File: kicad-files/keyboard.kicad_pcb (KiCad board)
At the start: 2 copper layers, 325 x 100 mm, 185 parts, among them J1 TYPE-C-31-M12_13, Q1 2N7002, Q2 2N7002, SW1 K2-1187SQ-A4SW-06, U1 STM32F411CEU6, U2 USBLC6-2SC6, U3 AT24C256C-SSHL-T, U4 SGM2007-3.3XN5/TR, Y1 TAXM8M4RFDCET2T

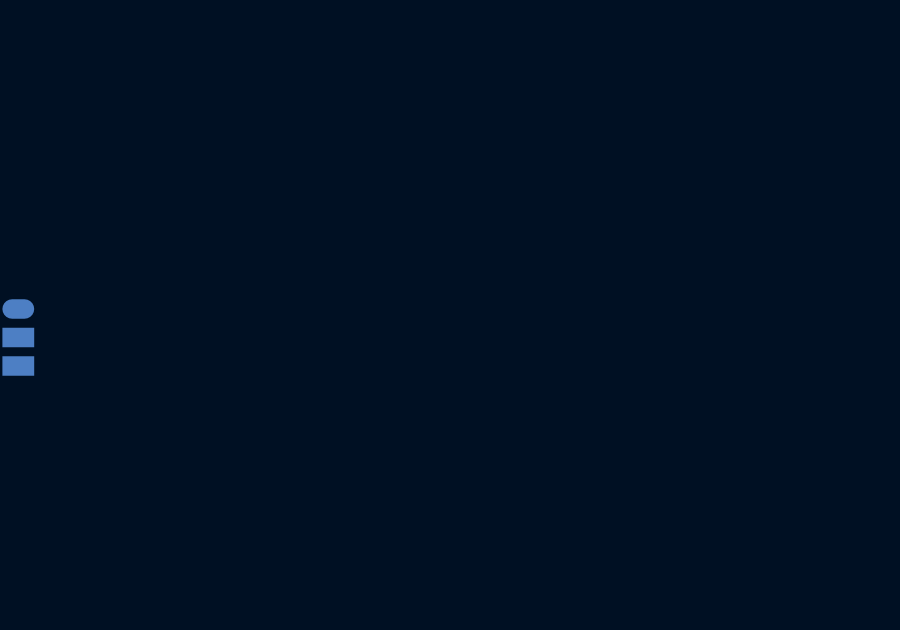
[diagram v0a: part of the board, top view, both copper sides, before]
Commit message: Added connector for DB
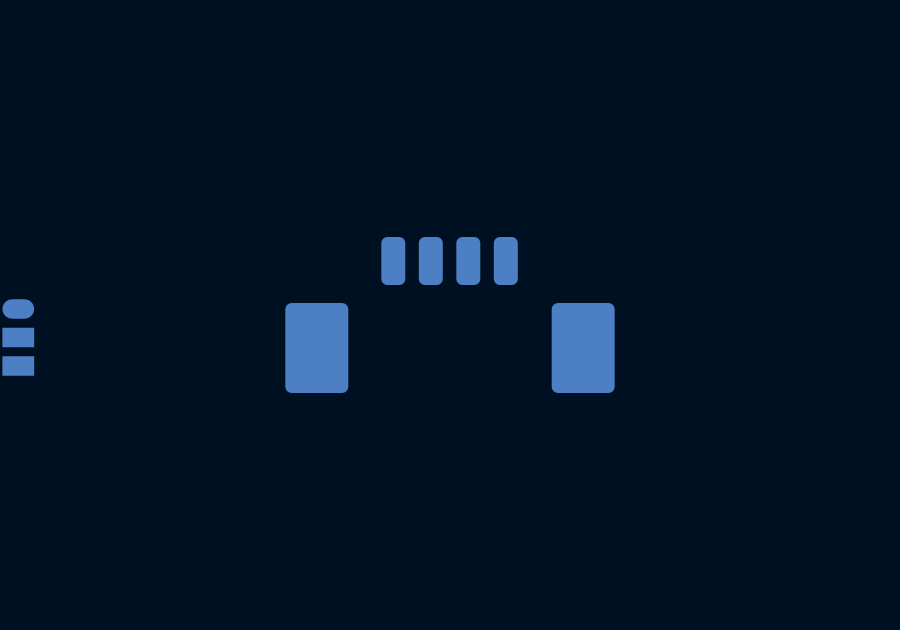
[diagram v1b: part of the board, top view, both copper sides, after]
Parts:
- added T1: 53261-0471, Legshark:Molex, PicoBlade, 53261, 4 Way, 1 Row, Right Angle PCB Header, B.Cu at (201.6, -28.7)
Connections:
- C3 pad 2: GND -> GND1
- C4 pad 2: GND -> GND1
- C5 pad 2: GND -> GND1
- FB1 pad 2: GND -> GND1
- J1 pad A1: GND -> GND1
- J1 pad B1: GND -> GND1
- R1 pad 2: GND -> GND1
- R2 pad 2: GND -> GND1
- R3 pad 1: GND -> GND1
- R4 pad 1: GND -> GND1
- SW1 pad 1: 3V3 -> unconnected-(SW1-A-Pad1)
- U2 pad 2: GND -> GND1
- U4 pad 2: GND -> GND1
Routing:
- net unconnected-(SW1-A-Pad1): track 0.00 -> 6.20 mm
- net 3V3: track 30.4 -> 24.2 mm

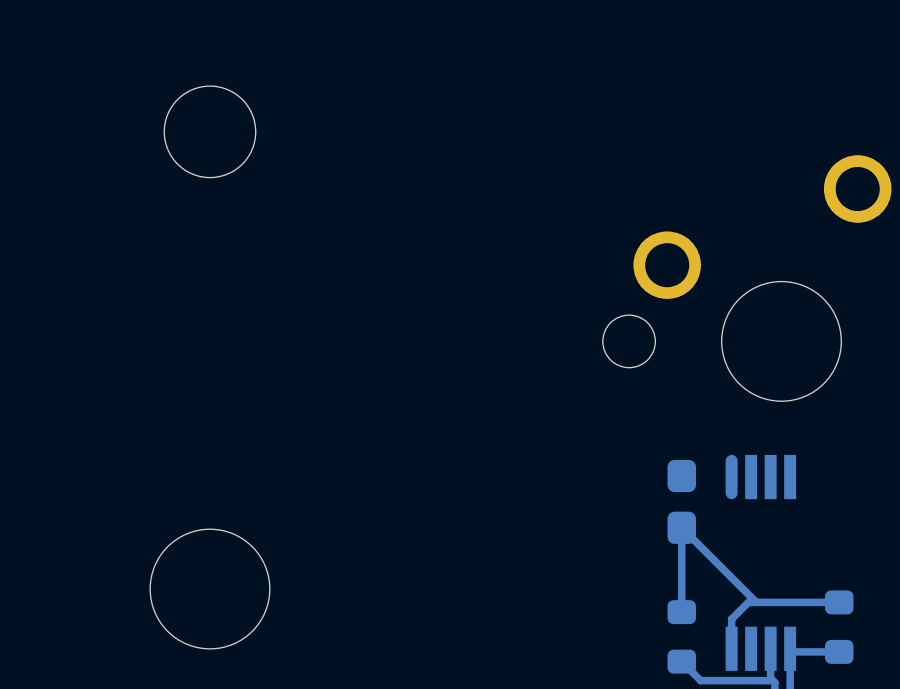
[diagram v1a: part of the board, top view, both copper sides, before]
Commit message: Added the cable header for DB to MB
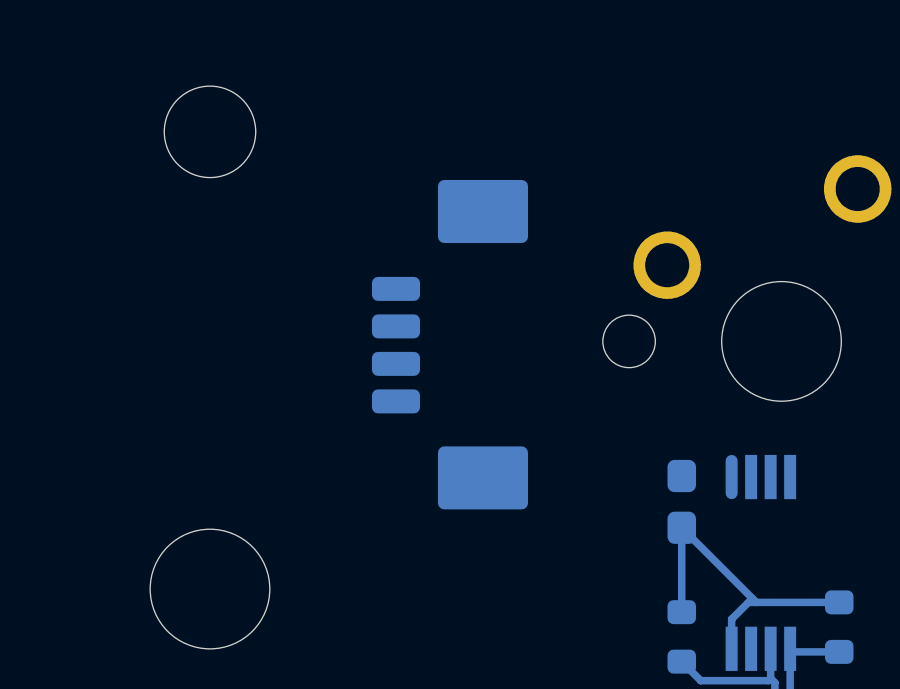
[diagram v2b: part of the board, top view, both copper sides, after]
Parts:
- added T2: 53261-0471, Legshark:Molex, PicoBlade, 53261, 4 Way, 1 Row, Right Angle PCB Header, B.Cu at (264.8, 50.3)
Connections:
- C5 pad 1: 3V3 -> Net-(D1-A)
- D1 pad 2: 3V3 -> Net-(D1-A)
- R4 pad 2: 3V3 -> Net-(D1-A)
- SW1 pad 1: unconnected-(SW1-A-Pad1) -> 3V3
- T1 pad 1: unconnected-(T1-P1-Pad1) -> Net-(D1-A)
- T1 pad 2: unconnected-(T1-P2-Pad2) -> Net-(T1-D-)
- T1 pad 3: unconnected-(T1-P3-Pad3) -> Net-(T1-D+)
- U2 pad 1: D+ -> Net-(T1-D+)
- U2 pad 3: D- -> Net-(T1-D-)
- U4 pad 5: 3V3 -> Net-(D1-A)
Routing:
- net unconnected-(SW1-A-Pad1): track 6.20 -> 0.00 mm
- net 3V3: track 24.2 -> 30.4 mm

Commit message: Added fill area for MB
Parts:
- moved D_46 16.1 mm to (310.0, 41.8)
- moved D_31 15.5 mm to (310.0, 22.8)
- moved D_15 15.3 mm to (310.2, 3.75)
- moved D_71 0.79 mm to (310.0, 80.0)
- moved T2 0.25 mm to (264.5, 50.3)
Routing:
- added copper zone on B.Cu, net GND
- added copper zone on F.Cu, net GND
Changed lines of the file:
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@@
   )
   (footprint "Diode_SMD:D_SOD-123" (layer "B.Cu")
-    (at 317 17.5)
+    (at 310.25 3.75)
     (descr "SOD-123")
     (tags "SOD-123")
@@
   )
   (footprint "Diode_SMD:D_SOD-123" (layer "B.Cu")
-    (at 316.75 36.75)
+    (at 310 22.75)
     (descr "SOD-123")
     (tags "SOD-123")
@@
   )
   (footprint "Legshark:Molex, PicoBlade, 53261, 4 Way, 1 Row, Right Angle PCB Header" (layer "B.Cu")
-    (at 264.775 50.3 -90)
+    (at 264.525 50.3 -90)
     (property "Sheetfile" "keyboard.kicad_sch")
     (property "Sheetname" "")
@@
       (polygon
         (pts
-          (xy 264.775 44.5)
-          (xy 264.775 56)
-          (xy 268.675 56)
-          (xy 268.675 44.5)
+          (xy 264.525 44.5)
+          (xy 264.525 56)
+          (xy 268.425 56)
+          (xy 268.425 44.5)
         )
       )
@@
   )
   (footprint "Diode_SMD:D_SOD-123" (layer "B.Cu")
-    (at 317 56.25)
+    (at 310 41.75)
     (descr "SOD-123")
     (tags "SOD-123")
@@
   )
   (footprint "Diode_SMD:D_SOD-123" (layer "B.Cu")
-    (at 310.75 80.25)
+    (at 310 80)
     (descr "SOD-123")
     (tags "SOD-123")
@@
   (segment (start 276.463108 60.39669) (end 276.463108 61.38419) (width 0.25) (layer "B.Cu") (net 151))
   (segment (start 276.463108 61.38419) (end 276.604919 61.526001) (width 0.25) (layer "B.Cu") (net 151))
+  (zone (net 104) (net_name "GND") (layer "F.Cu") (hatch edge 0.5)
+    (connect_pads (clearance 0.508))
+    (min_thickness 0.25) (filled_areas_thickness no)
+    (fill (thermal_gap 0.5) (thermal_bridge_width 0.5))
+    (polygon
+      (pts
+        (xy 0 0)
+        (xy 325 0)
+        (xy 325 100)
+        (xy 0 100)
+      )
+    )
+  )
+  (zone (net 104) (net_name "GND") (layer "B.Cu") (hatch edge 0.5)
+    (priority 1)
+    (connect_pads (clearance 0.508))
+    (min_thickness 0.25) (filled_areas_thickness no)
+    (fill (thermal_gap 0.5) (thermal_bridge_width 0.5))
+    (polygon
+      (pts
+        (xy 0 0)
+        (xy 325 0)
+        (xy 325 100)
+        (xy 0 100)
+      )
+    )
+  )
 )

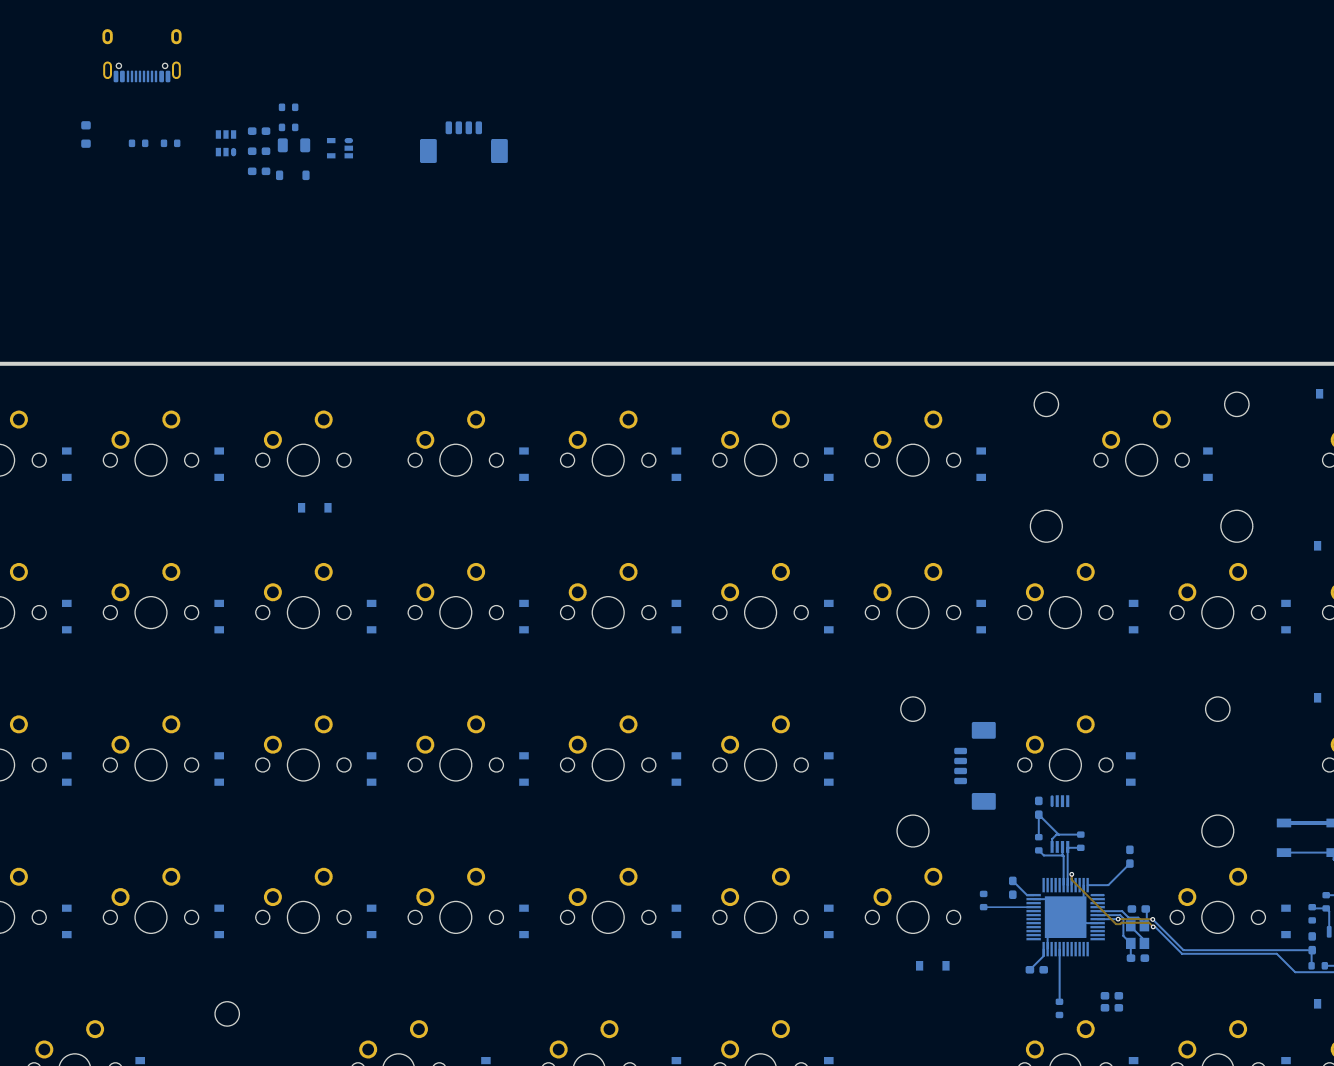
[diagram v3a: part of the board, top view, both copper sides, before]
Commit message: Connected all 3V3 to STM
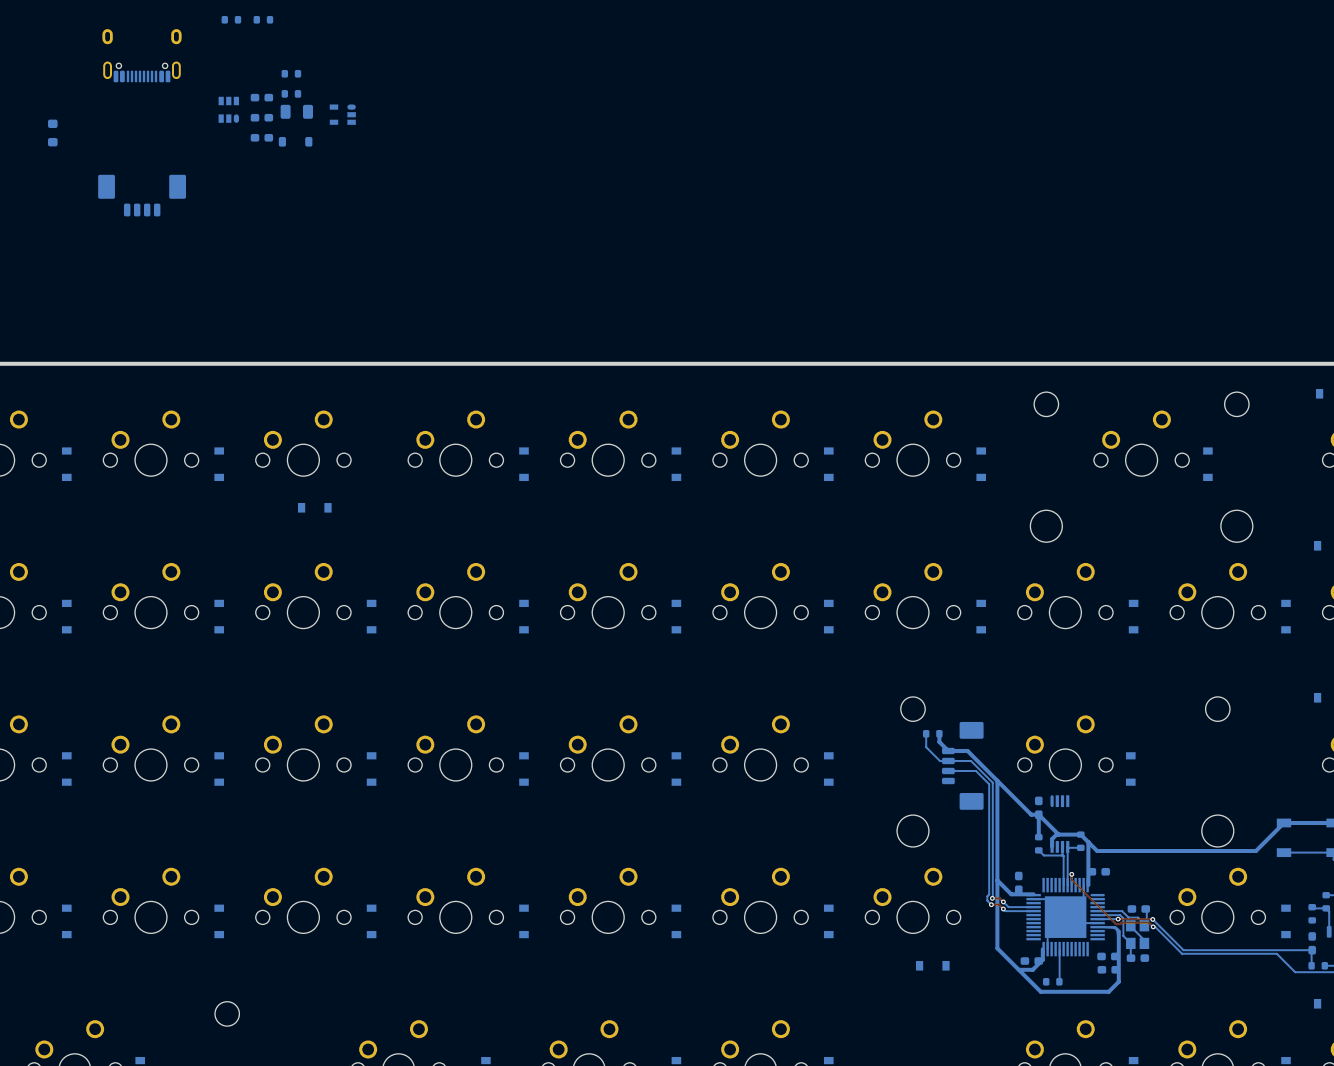
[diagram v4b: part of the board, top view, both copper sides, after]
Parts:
- moved T1 41.1 mm to (161.4, -20.0), turned to 0 degrees
- moved R5 21.8 mm to (260.2, 46.2), turned to 0 degrees
- moved R1 19.3 mm to (172.6, -43.0)
- moved R2 19.3 mm to (176.6, -43.0)
- moved C12 6.43 mm to (282.2, 74.1), turned to 0 degrees
- moved C9 4.32 mm to (281.0, 63.5), turned to 180 degrees
- moved C3 4.20 mm to (176.4, -33.3)
- moved R4 4.20 mm to (180.1, -33.7)
- moved C4 4.20 mm to (176.4, -30.8)
- moved C5 4.20 mm to (176.4, -28.2)
- moved D1 4.20 mm to (180.6, -27.8)
- moved F1 4.20 mm to (180.8, -31.5)
- moved R3 4.20 mm to (180.1, -36.2)
- moved U2 4.20 mm to (172.2, -31.8)
- moved U4 4.20 mm to (186.5, -31.1)
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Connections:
- T1 pad 2: Net-(T1-D-) -> Net-(T1-D+)
- T1 pad 3: Net-(T1-D+) -> Net-(T1-D-)
- T2 pad 2: D- -> D+
- T2 pad 3: D+ -> D-
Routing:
- net 3V3: track 30.4 -> 125.9 mm
- net D-: track 0.00 -> 26.8 mm, vias 0 -> 2
- net D+: track 6.25 -> 31.9 mm, vias 0 -> 2
- net Net-(U1-PB2--BOOT1): track 6.59 -> 4.10 mm
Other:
- board text added: "HARD RESET"

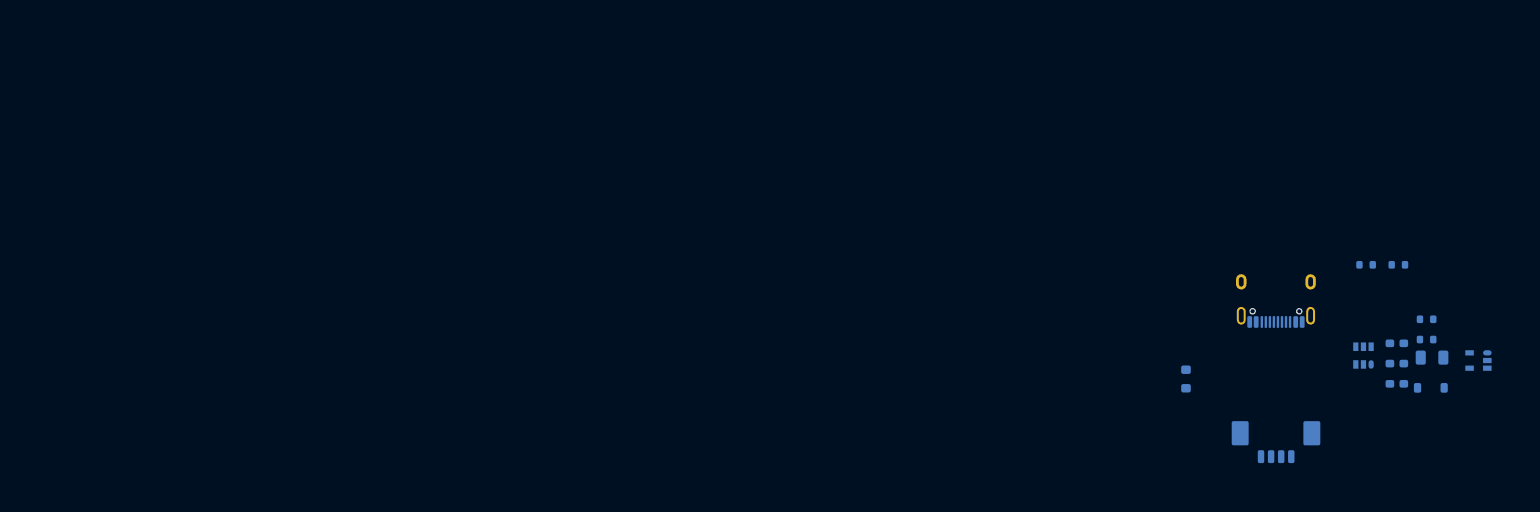
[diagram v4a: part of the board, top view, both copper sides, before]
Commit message: Started piecing together daughter board
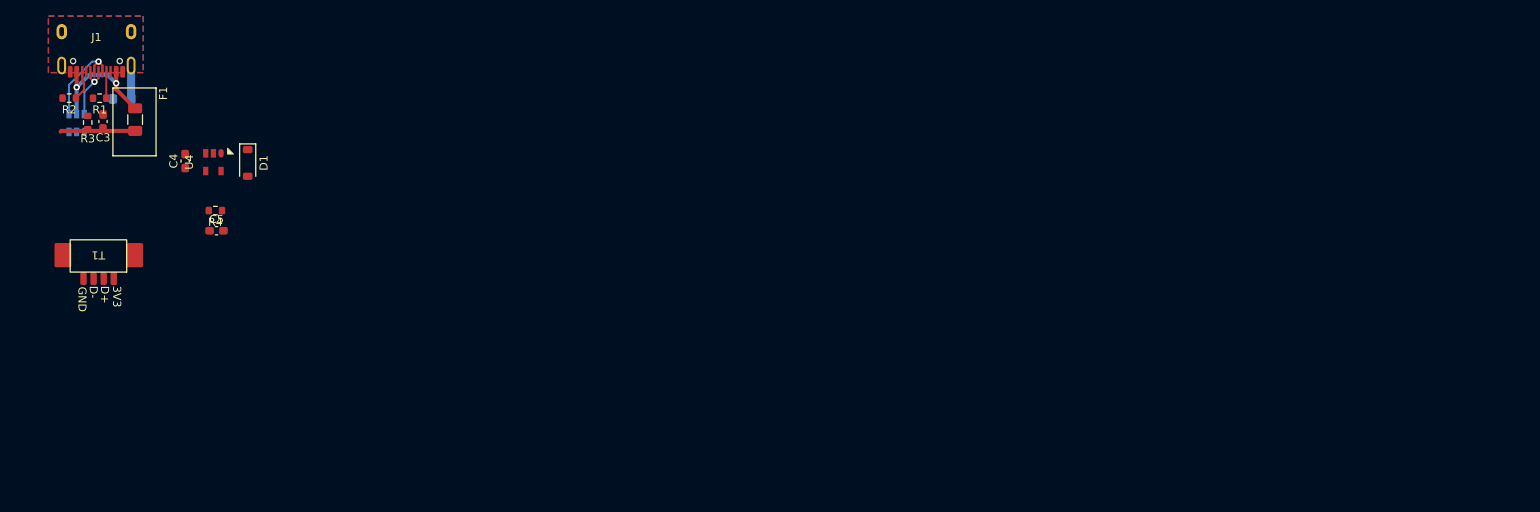
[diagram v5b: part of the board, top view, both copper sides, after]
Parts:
- C3, C4, C5, D1, F1, J1, R1, R2, R3, R4, T1, U4: moved to F.Cu
- moved R3 167.7 mm to (14.1, -60.6), turned to -90 degrees
- moved R2 166.0 mm to (11.8, -63.7), turned to 180 degrees
- moved F1 163.4 mm to (20.0, -61.0), turned to -90 degrees
- moved C3 162.7 mm to (16.0, -60.8), turned to 90 degrees
- moved U2 162.1 mm to (12.8, -60.6)
- moved U4 158.7 mm to (29.7, -55.7), turned to -90 degrees
- moved R1 158.3 mm to (15.6, -63.7)
- moved C4 152.3 mm to (26.2, -55.9), turned to 90 degrees
- moved R4 151.0 mm to (29.9, -49.7)
- moved J1 149.5 mm to (15.2, -66.2), turned to 180 degrees
- moved D1 149.3 mm to (34.0, -55.6), turned to -90 degrees
- moved T1 147.7 mm to (15.4, -42.1), turned to 180 degrees
- moved C5 147.5 mm to (30.1, -47.2), turned to 0 degrees
- moved FB1 136.4 mm to (18.4, -63.6), turned to 180 degrees
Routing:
- net Net-(U2-VBUS): track 0.00 -> 16.7 mm, vias 0 -> 2
- net Net-(J1-D--PadA7): track 0.00 -> 11.3 mm, vias 0 -> 1
- net 5V: track 0.00 -> 9.29 mm
- net Net-(J1-D+-PadA6): track 0.00 -> 7.33 mm, vias 0 -> 1
- net GNDPWR: track 0.00 -> 4.23 mm
- net Net-(J1-CC2): track 0.00 -> 3.81 mm
- net Net-(J1-CC1): track 0.00 -> 3.28 mm
- added copper zone on B.Cu, net GNDPWR
- added copper zone on F.Cu, net GNDPWR

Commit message: Finished ic placement for daughter board
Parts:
- moved C3 345.2 mm to (343.5, 48.2)
- moved FB1 345.2 mm to (345.9, 45.4)
- moved J1 345.2 mm to (342.7, 42.8)
- moved R1 345.2 mm to (343.1, 45.3)
- moved R2 345.2 mm to (339.3, 45.3)
- moved R3 345.2 mm to (341.6, 48.4)
- moved U2 345.2 mm to (340.2, 48.4)
- moved F1 344.7 mm to (347.0, 48.0)
- moved T1 342.1 mm to (342.5, 58.3), turned to 0 degrees
- moved C4 329.8 mm to (337.9, 51.9), turned to 180 degrees
- moved D1 326.4 mm to (342.2, 51.7), turned to 180 degrees
- moved R4 326.4 mm to (339.5, 53.8), turned to 0 degrees
- moved C5 325.9 mm to (339.3, 55.5), turned to 180 degrees
- moved U4 325.5 mm to (338.0, 48.6)
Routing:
- net Net-(T1-D-): track 0.00 -> 10.7 mm, vias 0 -> 1
- net 5V: track 9.29 -> 18.9 mm
- net Net-(T1-D+): track 0.00 -> 8.93 mm, vias 0 -> 1
- net Net-(D1-A): track 0.00 -> 8.46 mm
- net Net-(U4-BP/FB): track 0.00 -> 2.88 mm
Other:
- board size 325 x 100 mm -> 349.5 x 100 mm
